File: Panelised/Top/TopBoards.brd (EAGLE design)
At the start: 120.7 x 66.5 mm, 30 parts, among them K1 HF46105, K11 61004021821, K2 HF46105, K3 HF46105, K4 HF46105, P1 DF11-06-2DSA, Q1 691131710002, Q11 BS170, Q2 691131710002, Q3 691131710002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

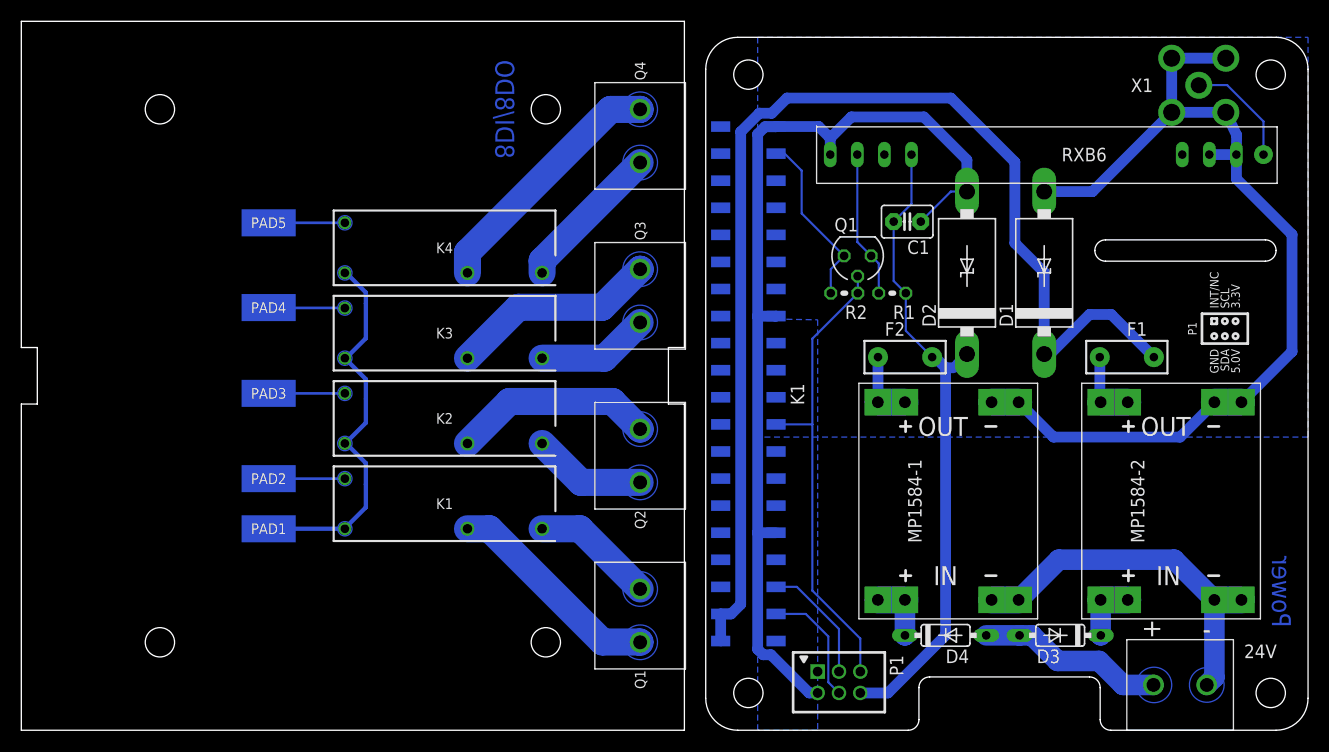
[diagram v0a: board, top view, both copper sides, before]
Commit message: Remove AGND supply, since DC/DC converter use same GND signal.
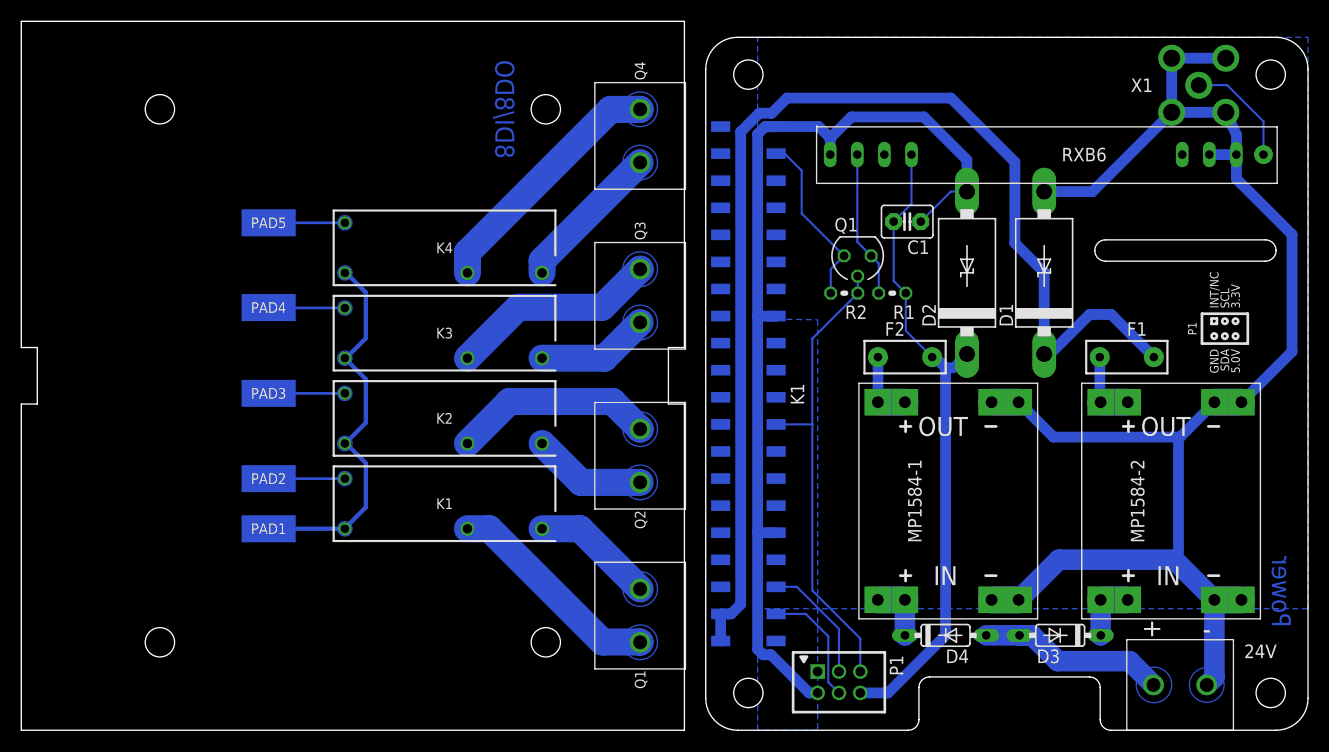
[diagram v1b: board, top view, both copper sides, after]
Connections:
- removed net AGND: 24V.1, MP1584-1.IN-0, MP1584-1.IN-1, MP1584-2.IN-0, MP1584-2.IN-1
- net GND: now also 24V.1, MP1584-1.IN-0, MP1584-1.IN-1, MP1584-2.IN-0, MP1584-2.IN-1
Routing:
- net GND: track 182.5 -> 229.3 mm
- net AGND: track 35.1 -> 0.00 mm
- removed copper zone on layer 16, net AGND
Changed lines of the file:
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@@
 <contactref element="MP1584-1" pad="OUT-0"/>
 <polygon width="1.016" layer="16" isolate="0.4064" thermals="no">
-<vertex x="58.5" y="27.5"/>
-<vertex x="6.87" y="27.5"/>
+<vertex x="58.5" y="11.4"/>
+<vertex x="6.87" y="11.4"/>
 <vertex x="6.87" y="65"/>
 <vertex x="58.5" y="65"/>
@@
 <vertex x="6.87" y="0"/>
 </polygon>
-</signal>
-<signal name="+24V">
-<contactref element="D3" pad="A"/>
-<contactref element="D4" pad="A"/>
-<contactref element="24V" pad="2"/>
-<polygon width="0.35" layer="16" isolate="0.254" thermals="no">
-<vertex x="45.3" y="3.15" curve="180"/>
-<vertex x="42.8" y="5.35" curve="180"/>
-</polygon>
-<wire x1="41.15" y1="4.25" x2="38.9" y2="6.5" width="1.9304" layer="16"/>
-<wire x1="38.9" y1="6.5" x2="35" y2="6.5" width="1.9304" layer="16"/>
-<wire x1="35" y1="6.5" x2="32.6" y2="8.9" width="1.9304" layer="16"/>
-<wire x1="32.6" y1="8.9" x2="31.44" y2="8.9" width="1.9304" layer="16"/>
-<wire x1="44" y1="4.25" x2="41.15" y2="4.25" width="1.9304" layer="16"/>
-<wire x1="28.31" y1="8.9" x2="31.44" y2="8.9" width="1.9304" layer="16"/>
-</signal>
-<signal name="AGND">
 <contactref element="MP1584-2" pad="IN-0"/>
 <contactref element="MP1584-1" pad="IN-0"/>
 <contactref element="24V" pad="1"/>
-<polygon width="0.35" layer="16" thermals="no">
-<vertex x="50.2" y="3.15" curve="180"/>
-<vertex x="47.8" y="5.35" curve="180"/>
-</polygon>
 <contactref element="MP1584-2" pad="IN-1"/>
 <contactref element="MP1584-1" pad="IN-1"/>
@@
 <wire x1="31.354" y1="12.229" x2="35.125" y2="16" width="1.9304" layer="16"/>
 <wire x1="35.125" y1="16" x2="45.943" y2="16" width="1.9304" layer="16"/>
+<wire x1="46.3484" y1="27.1624" x2="46.3484" y2="16.7978" width="1.016" layer="16"/>
+<wire x1="46.3484" y1="16.7978" x2="45.943" y2="16" width="1.016" layer="16"/>
+<wire x1="46.3484" y1="27.1624" x2="46.5" y2="27.5" width="0.1524" layer="16"/>
+<polygon width="0.35" layer="16" thermals="no">
+<vertex x="50.2" y="3.15" curve="180"/>
+<vertex x="47.8" y="5.35" curve="180"/>
+</polygon>
+</signal>
+<signal name="+24V">
+<contactref element="D3" pad="A"/>
+<contactref element="D4" pad="A"/>
+<contactref element="24V" pad="2"/>
+<polygon width="0.35" layer="16" isolate="0.254" thermals="no">
+<vertex x="45.3" y="3.15" curve="180"/>
+<vertex x="42.8" y="5.35" curve="180"/>
+</polygon>
+<wire x1="32.6" y1="8.9" x2="32.1" y2="8.9" width="1.9304" layer="16"/>
+<wire x1="32.1" y1="8.9" x2="31.44" y2="8.9" width="1.9304" layer="16"/>
+<wire x1="28.31" y1="8.9" x2="31.44" y2="8.9" width="1.9304" layer="16"/>
+<wire x1="44" y1="4.25" x2="41.77" y2="6.48" width="1.9304" layer="16"/>
+<wire x1="41.77" y1="6.48" x2="35.02" y2="6.48" width="1.9304" layer="16"/>
+<wire x1="35.02" y1="6.48" x2="32.6" y2="8.9" width="1.9304" layer="16"/>
+<wire x1="32.6" y1="8.9" x2="32.1" y2="8.9" width="1.9304" layer="16"/>
 </signal>
 <signal name="N$21">

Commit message: Increase ground plane.
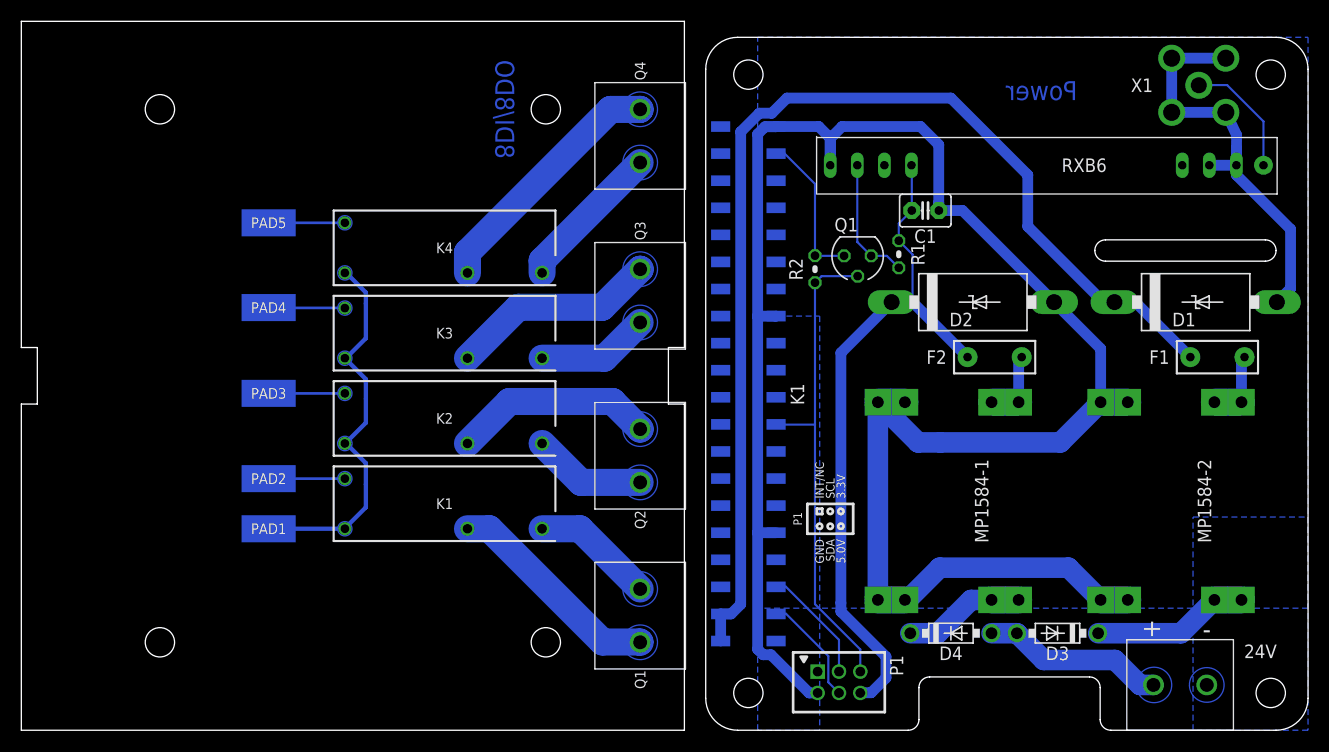
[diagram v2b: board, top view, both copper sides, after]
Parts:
- D3, D4: value 1N4148DO35-7 -> SB160; device diode:DO35-7 -> diode:DO41-7.6
- moved D1 14.5 mm to (48.0, 40.2), turned to 0 degrees
- moved F1 8.50 mm to (50.0, 35.0), turned to 0 degrees
- moved F2 8.40 mm to (29.1, 35.0), turned to 180 degrees
- moved R1 3.70 mm to (20.1, 44.6), turned to 270 degrees
- moved R2 3.55 mm to (12.2, 43.2), turned to 270 degrees
- moved D2 2.80 mm to (27.1, 40.2), turned to 0 degrees
- moved C1 1.99 mm to (22.6, 48.8)
- moved RXB6 1.00 mm to (34.0, 53.0)
- moved D4 0.54 mm to (25.0, 9.10)
- moved D3 0.32 mm to (35.0, 9.10)
- flipped MP1584-1 to the bottom
- flipped MP1584-2 to the bottom
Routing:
- net N$71: track 5.89 -> 14.8 mm
- net N$51: track 111.3 -> 105.5 mm
- net N$91: track 5.87 -> 11.5 mm
- net N$21: track 60.8 -> 65.1 mm
- net N$69: track 16.7 -> 14.3 mm
- net N$111: track 44.3 -> 46.3 mm
- net N$3: track 13.8 -> 12.1 mm
- net N$121: track 11.5 -> 10.4 mm
- net N$81: track 10.6 -> 11.6 mm
- net +24V: track 18.1 -> 17.2 mm
- net GND: track 229.3 -> 228.5 mm
- net N$15: track 11.5 -> 11.0 mm
